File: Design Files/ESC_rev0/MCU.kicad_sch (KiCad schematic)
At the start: 39 parts, among them J1 Conn_01x08, J2 Conn_01x06, J3 Conn_01x03, SW1 SW_DIP_x01, U4 STM32F405RGTx, Y1 Crystal

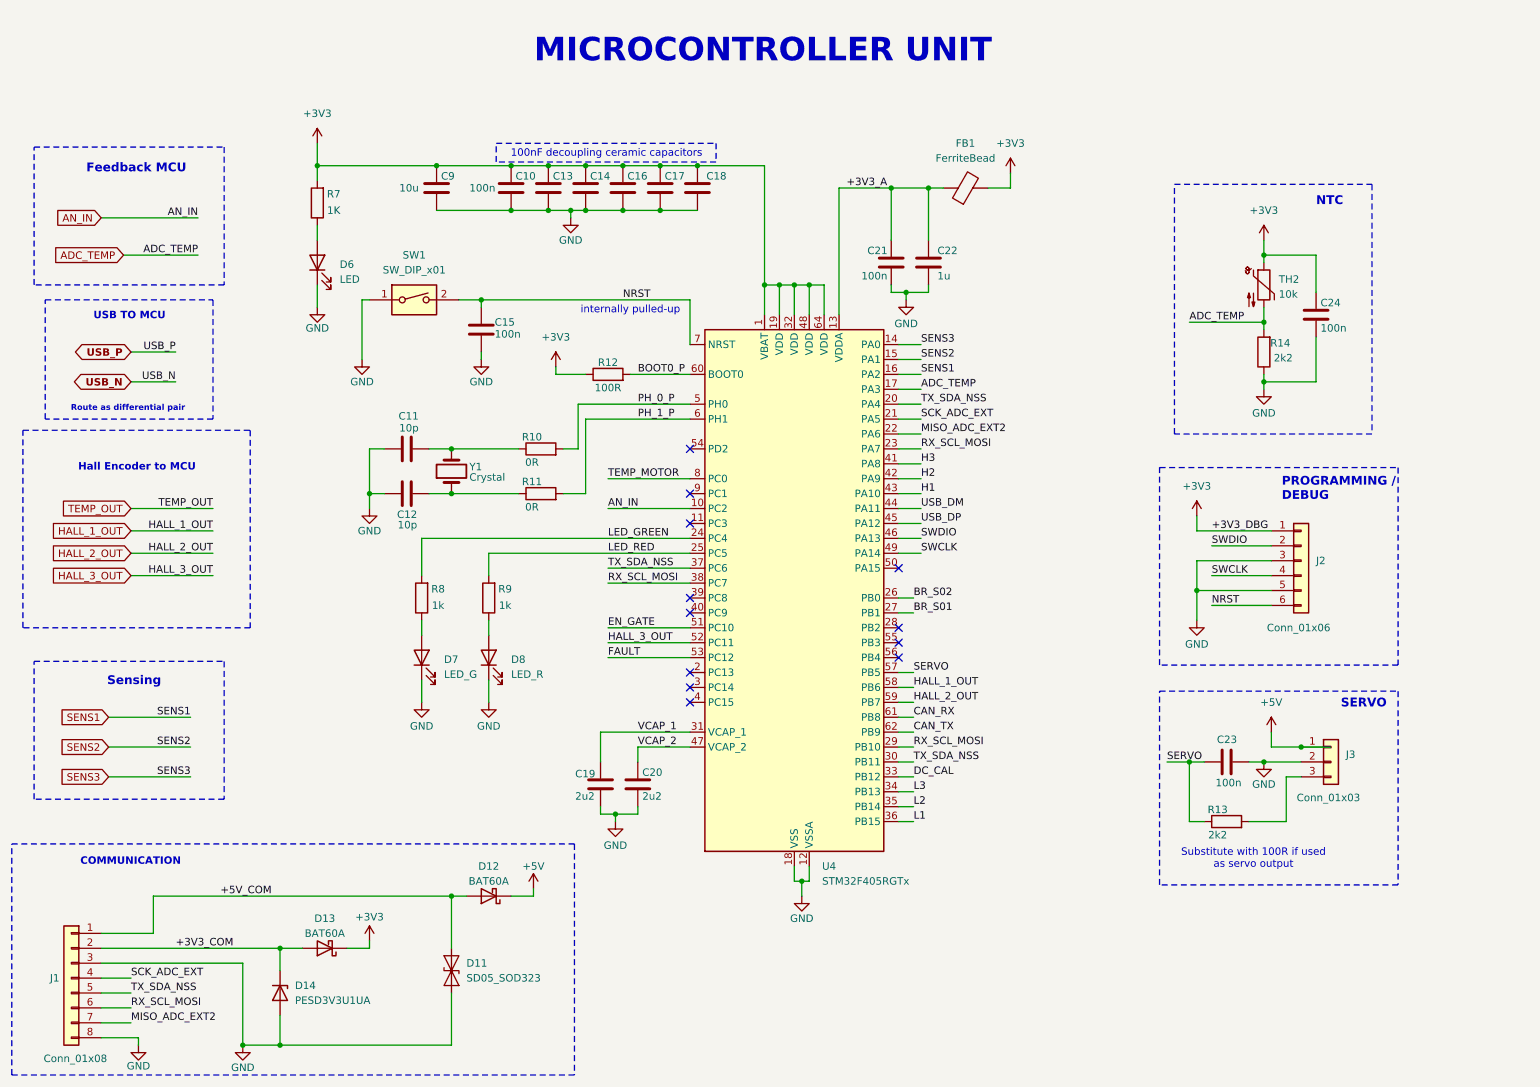
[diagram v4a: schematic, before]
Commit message: update 13
assigned all footprints (provisionally) and imported them - errors and warning occurred, must be corrected in the future
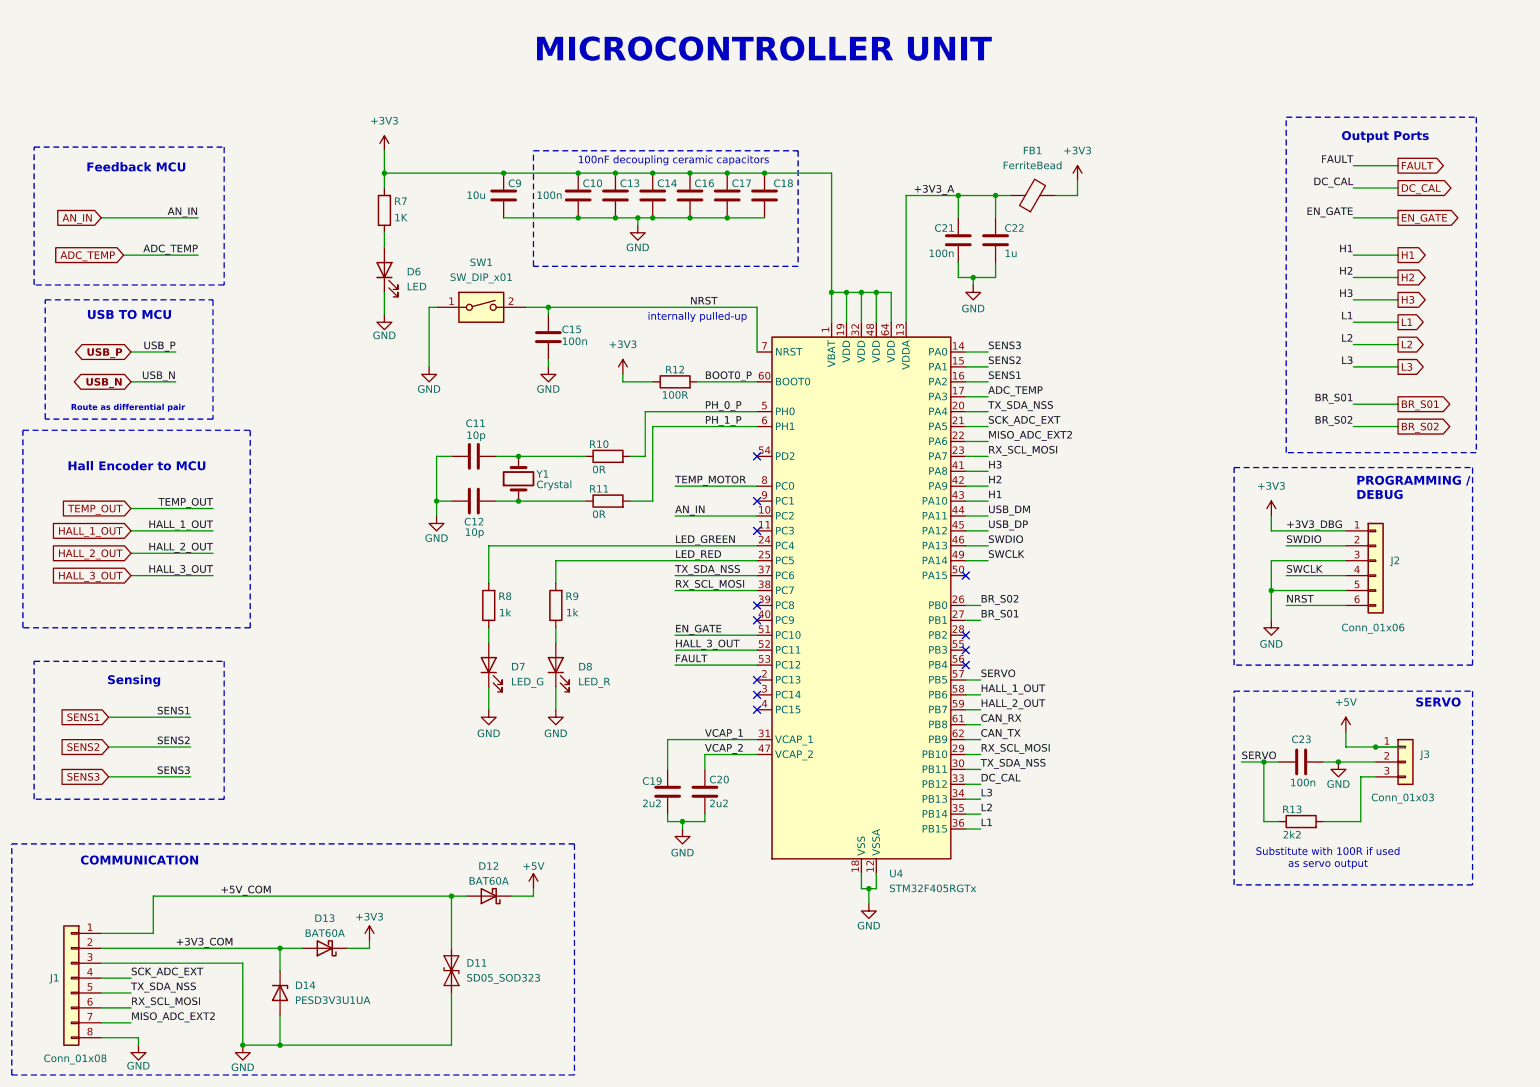
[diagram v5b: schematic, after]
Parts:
- removed C24: 100n, Capacitor_SMD:C_0201_0603Metric, symbol Device:C
- removed R14: 2k2, symbol Device:R
- removed TH2: 10k, symbol Device:Thermistor_NTC
- J1: footprint (none) -> Connector_PinHeader_2.00mm:PinHeader_1x08_P2.00mm_Vertical
- J2: footprint (none) -> Connector_PinHeader_2.00mm:PinHeader_1x06_P2.00mm_Vertical
- J3: footprint (none) -> Connector_PinHeader_2.00mm:PinHeader_1x03_P2.00mm_Vertical
- R10, R11, R12, R13, R7, R8, R9: footprint (none) -> Resistor_SMD:R_0603_1608Metric
- SW1: footprint (none) -> Button_Switch_SMD:SW_DIP_SPSTx01_Slide_6.7x4.1mm_W6.73mm_P2.54mm_LowProfile_JPin
- Y1: footprint (none) -> Crystal:Crystal_HC50_Vertical
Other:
- note added: "Output Ports"
- note removed: "NTC"
- moved on the sheet: C10, C11, C12, C13, C14, C15, C16, C17, C18, C19, C20, C21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

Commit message: update 14
Circuits separated by schematic pages. Replaced crystal footprint.
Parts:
- Y1: footprint Crystal:Crystal_HC50_Vertical -> Crystal:Crystal_SMD_0603-4Pin_6.0x3.5mm_HandSoldering
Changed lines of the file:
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@@
 			)
 		)
-		(property "Footprint" "Crystal:Crystal_HC50_Vertical"
+		(property "Footprint" "Crystal:Crystal_SMD_0603-4Pin_6.0x3.5mm_HandSoldering"
 			(at 104.14 93.98 0)
 			(effects

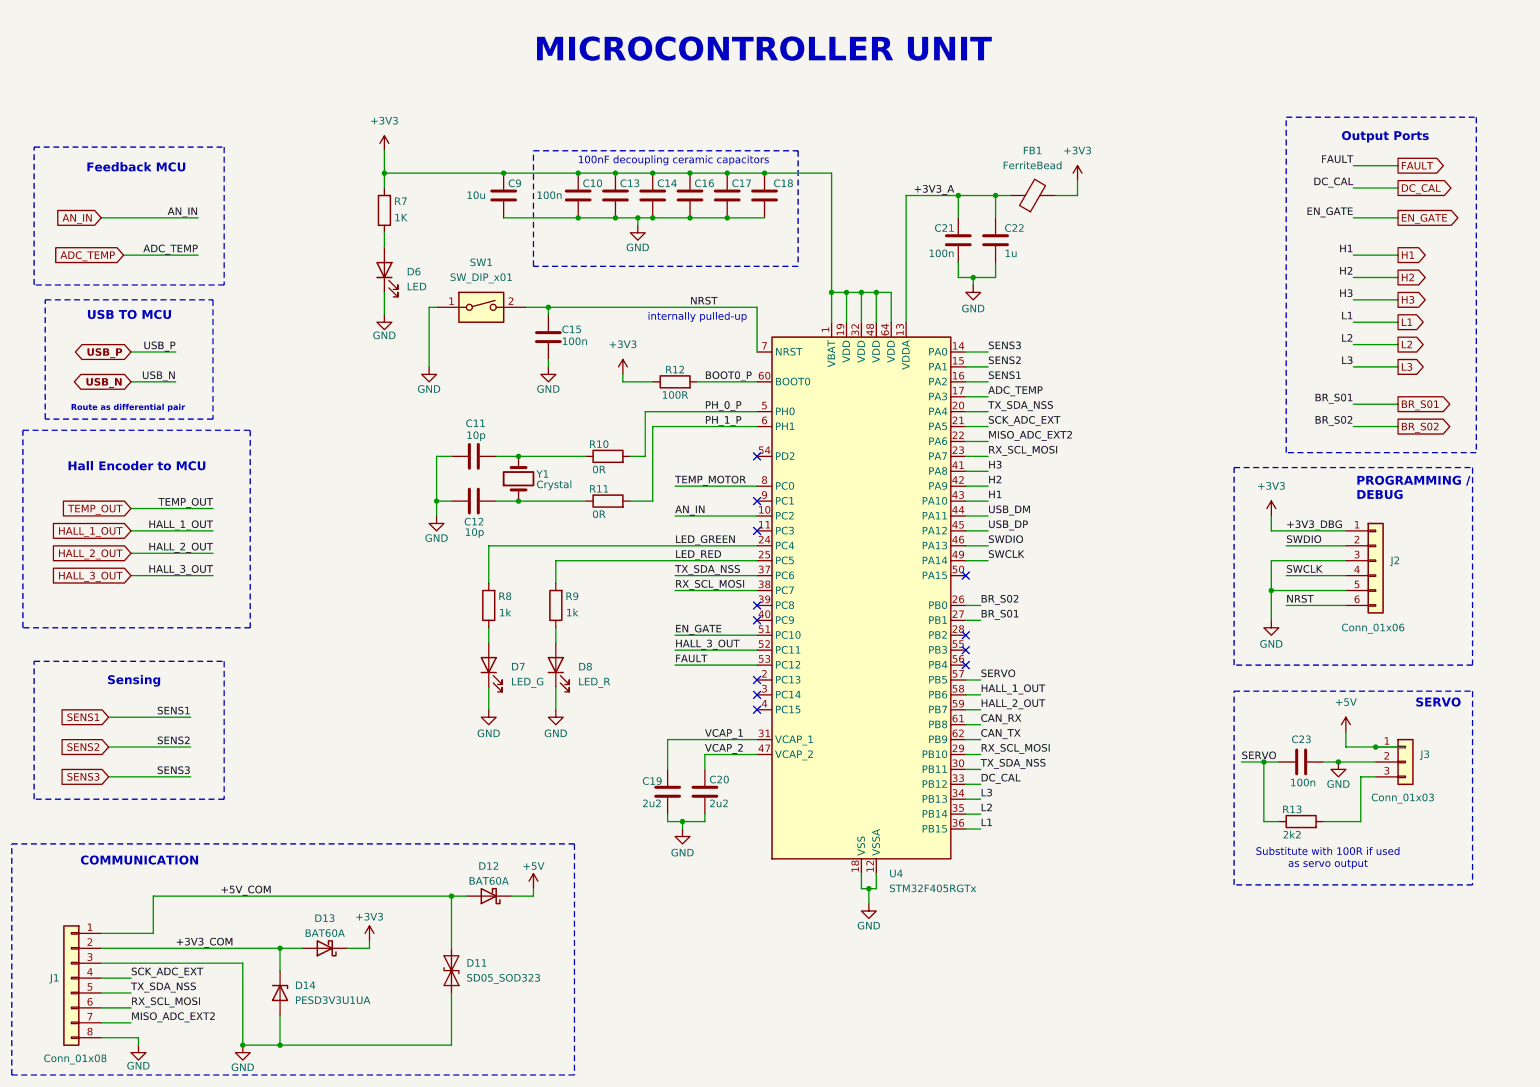
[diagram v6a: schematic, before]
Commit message: update 15
Simple connectors replaced by smd connectors (downloaded). Connectors were placed in edges of the board.
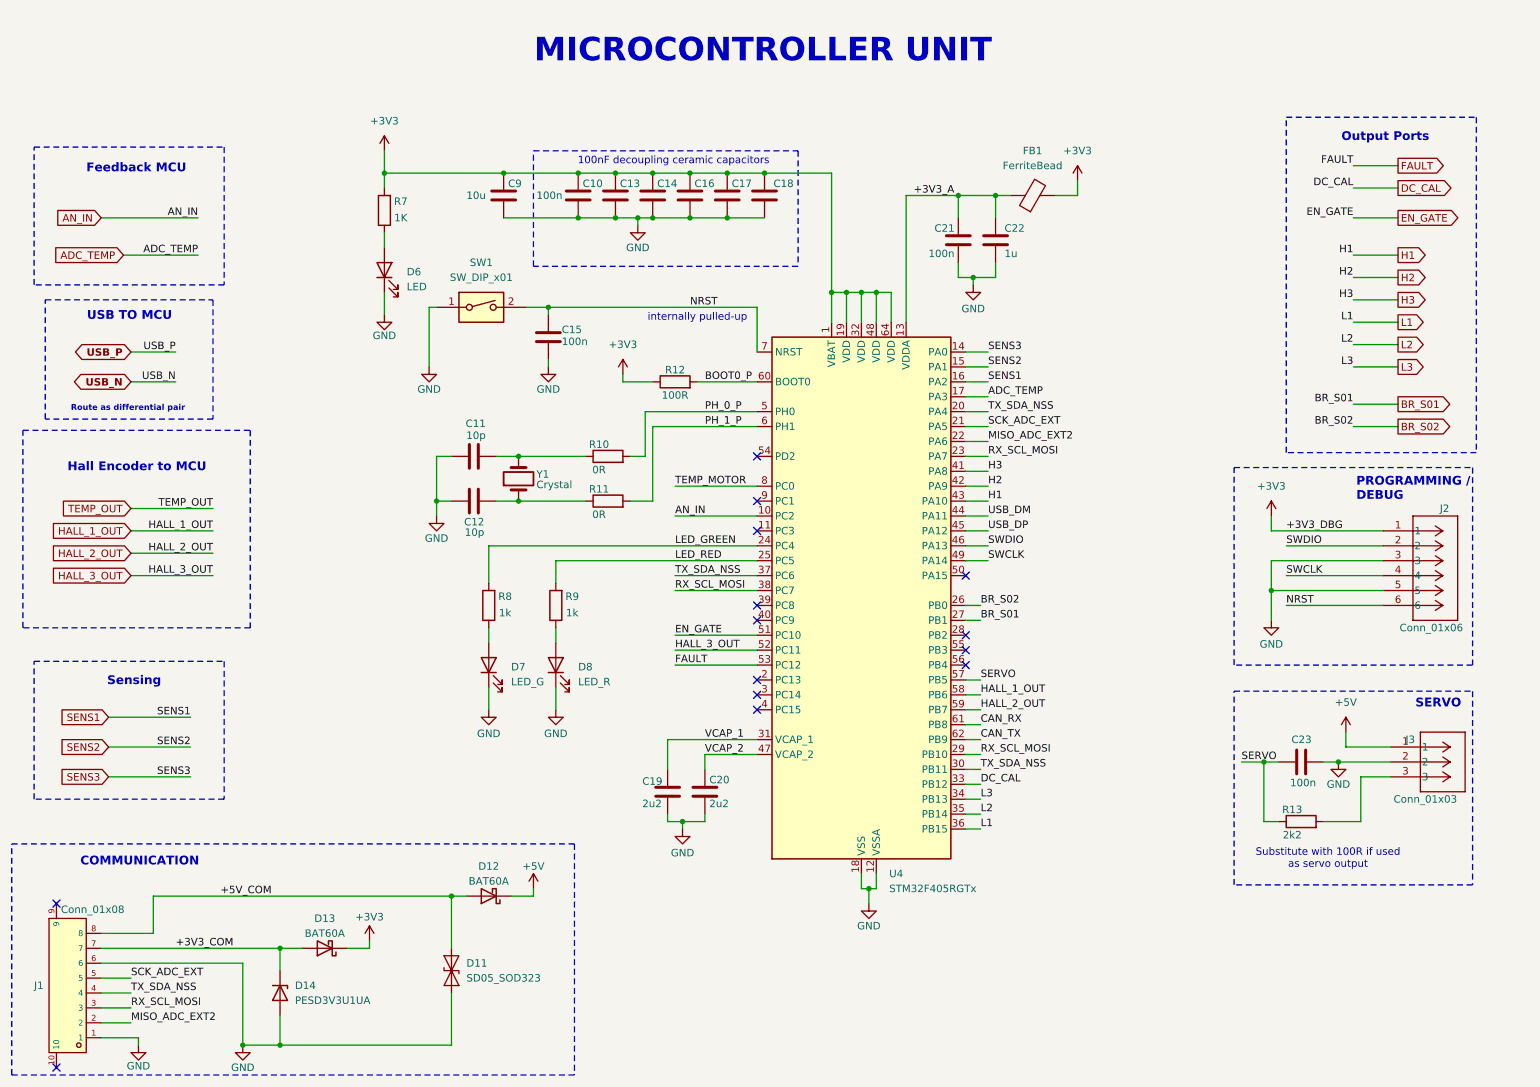
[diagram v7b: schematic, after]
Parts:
- J1: footprint Connector_PinHeader_2.00mm:PinHeader_1x08_P2.00mm_Vertical -> HX25003-8AWB:CONN-SMD_8P-P2.50_HX25003-8AWB; symbol Connector_Generic:Conn_01x08 -> HX25003-8AWB:HX25003-8AWB; LCSC (none) -> C442367
- J2: footprint Connector_PinHeader_2.00mm:PinHeader_1x06_P2.00mm_Vertical -> CONN_S6B-XH-SM4-TB_JST; symbol Connector_Generic:Conn_01x06 -> S6B-XH-SM4-TB:S6B-XH-SM4-TB
- J3: footprint Connector_PinHeader_2.00mm:PinHeader_1x03_P2.00mm_Vertical -> CONN3_S3B-XH_JST; symbol Connector_Generic:Conn_01x03 -> S3B-XH-SM4-TB:S3B-XH-SM4-TB
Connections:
- net +3V3_COM: now also J1.7; no longer J1.2 (Pin_2)
- net +5V_COM: now also J1.8; no longer J1.1 (Pin_1)
- net GND: now also J1.1, J1.6; no longer J1.3 (Pin_3), J1.8 (Pin_8)
- net MISO_ADC_EXT2: now also J1.2; no longer J1.7 (Pin_7)
- net RX_SCL_MOSI: now also J1.3; no longer J1.6 (Pin_6)
- net SCK_ADC_EXT: now also J1.5; no longer J1.4 (Pin_4)
- net TX_SDA_NSS: now also J1.4; no longer J1.5 (Pin_5)
- no-connect marks 12 -> 14
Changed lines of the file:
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@@
 	)
 	(junction
-		(at 250.19 139.7)
-		(diameter 0)
-		(color 0 0 0 0)
-	)
-	(junction
 		(at 114.3 41.91)
 		(diameter 0)
@@
 	)
 	(no_connect
+		(at 25.4 166.37)
+	)
+	(no_connect
 		(at 144.78 115.57)
 	)
@@
 	)
 	(no_connect
+		(at 25.4 194.31)
+	)
+	(no_connect
 		(at 144.78 133.35)
 	)
@@
 	(wire
 		(pts
+			(xy 245.11 139.7) (xy 252.73 139.7)
+		)
+		(stroke
+			(width 0)
+			(type default)
+		)
+	)
+	(wire
+		(pts
 			(xy 157.48 41.91) (xy 157.48 62.23)
 		)
@@
 	(wire
 		(pts
-			(xy 232.41 113.03) (xy 245.11 113.03)
+			(xy 232.41 113.03) (xy 251.46 113.03)
 		)
 		(stroke
@@
 	(wire
 		(pts
-			(xy 243.84 142.24) (xy 250.19 142.24)
+			(xy 243.84 142.24) (xy 252.73 142.24)
 		)
 		(stroke
@@
 	(wire
 		(pts
-			(xy 255.27 139.7) (xy 250.19 139.7)
-		)
-		(stroke
-			(width 0)
-			(type default)
-		)
-	)
-	(wire
-		(pts
 			(xy 165.1 62.23) (xy 165.1 67.31)
 		)
@@
 	(wire
 		(pts
-			(xy 234.95 115.57) (xy 245.11 115.57)
+			(xy 234.95 115.57) (xy 251.46 115.57)
 		)
 		(stroke
@@
 	(wire
 		(pts
-			(xy 234.95 110.49) (xy 245.11 110.49)
+			(xy 234.95 110.49) (xy 251.46 110.49)
 		)
 		(stroke
@@
 	(wire
 		(pts
-			(xy 247.65 144.78) (xy 250.19 144.78)
+			(xy 247.65 144.78) (xy 252.73 144.78)
 		)
 		(stroke
@@
 	(wire
 		(pts
-			(xy 250.19 139.7) (xy 245.11 139.7)
-		)
-		(stroke
-			(width 0)
-			(type default)
-		)
-	)
-	(wire
-		(pts
 			(xy 120.65 41.91) (xy 127 41.91)
 		)
@@
 	(wire
 		(pts
-			(xy 234.95 105.41) (xy 245.11 105.41)
+			(xy 234.95 105.41) (xy 251.46 105.41)
 		)
 		(stroke
@@
 	(wire
 		(pts
-			(xy 57.15 176.53) (xy 33.02 176.53)
+			(xy 180.34 133.35) (xy 182.88 133.35)
 		)
 		(stroke
@@
 	(wire
 		(pts
-			(xy 180.34 133.35) (xy 182.88 133.35)
+			(xy 241.3 142.24) (xy 243.84 142.24)
 		)
 		(stroke
@@
 	(wire
 		(pts
-			(xy 241.3 142.24) (xy 243.84 142.24)
+			(xy 227.33 142.24) (xy 231.14 142.24)
 		)
 		(stroke
@@
 	(wire
 		(pts
-			(xy 227.33 142.24) (xy 231.14 142.24)
+			(xy 33.02 186.69) (xy 38.1 186.69)
 		)
 		(stroke
@@
 	(wire
 		(pts
-			(xy 33.02 186.69) (xy 38.1 186.69)
+			(xy 63.5 190.5) (xy 57.15 190.5)
 		)
 		(stroke
@@
 	(wire
 		(pts
-			(xy 63.5 190.5) (xy 57.15 190.5)
+			(xy 33.02 176.53) (xy 57.15 176.53)
 		)
 		(stroke
@@
 	(wire
 		(pts
-			(xy 245.11 107.95) (xy 232.41 107.95)
+			(xy 232.41 107.95) (xy 251.46 107.95)
 		)
 		(stroke
@@
 	(wire
 		(pts
-			(xy 245.11 102.87) (xy 232.41 102.87)
+			(xy 232.41 102.87) (xy 251.46 102.87)
 		)
 		(stroke
@@
 	)
 	(symbol
-		(lib_id "Connector_Generic:Conn_01x06")
-		(at 250.19 107.95 0)
+		(lib_id "S6B-XH-SM4-TB:S6B-XH-SM4-TB")
+		(at 251.46 102.87 0)
 		(unit 1)
 		(exclude_from_sim no)
@@
 		(dnp no)
 		(property "Reference" "J2"
-			(at 252.73 107.9499 0)
+			(at 261.112 99.06 0)
 			(effects
 				(font
@@
 		)
 		(property "Value" "Conn_01x06"
-			(at 244.348 119.38 0)
+			(at 254.254 119.38 0)
 			(effects
 				(font
@@
 			)
 		)
-		(property "Footprint" "Connector_PinHeader_2.00mm:PinHeader_1x06_P2.00mm_Vertical"
-			(at 250.19 107.95 0)
+		(property "Footprint" "CONN_S6B-XH-SM4-TB_JST"
+			(at 254.762 119.634 0)
 			(effects
 				(font
 					(size 1.27 1.27)
+					(italic yes)
 				)
 				(hide yes)
 			)
 		)
-		(property "Datasheet" "~"
-			(at 250.19 107.95 0)
+		(property "Datasheet" "S6B-XH-SM4-TB"
+			(at 249.174 99.314 0)
 			(effects
 				(font
 					(size 1.27 1.27)
+					(italic yes)
 				)
 				(hide yes)
@@
 		)
 		(property "Description" "Generic connector, single row, 01x06, script generated (kicad-library-utils/schlib/autogen/connector/)"
-			(at 250.19 107.95 0)
+			(at 251.46 102.87 0)
 			(effects
 				(font
@@
 	)
 	(symbol
-		(lib_id "Connector_Generic:Conn_01x03")
-		(at 255.27 142.24 0)
+		(lib_id "S3B-XH-SM4-TB:S3B-XH-SM4-TB")
+		(at 252.73 139.7 0)
 		(unit 1)
 		(exclude_from_sim no)
@@
 		(dnp no)
 		(property "Reference" "J3"
-			(at 257.81 140.9699 0)
+			(at 255.27 138.4299 0)
 			(effects
 				(font
@@
 		)
 		(property "Value" "Conn_01x03"
-			(at 249.428 148.336 0)
+			(at 253.238 148.59 0)
 			(effects
 				(font
@@
 			)
 		)
-		(property "Footprint" "Connector_PinHeader_2.00mm:PinHeader_1x03_P2.00mm_Vertical"
-			(at 255.27 142.24 0)
+		(property "Footprint" "CONN3_S3B-XH_JST"
+			(at 252.73 139.7 0)
 			(effects
 				(font
 					(size 1.27 1.27)
+					(italic yes)
 				)
 				(hide yes)
 			)
 		)
-		(property "Datasheet" "~"
-			(at 255.27 142.24 0)
+		(property "Datasheet" "S3B-XH-SM4-TB"
+			(at 252.73 139.7 0)
 			(effects
 				(font
 					(size 1.27 1.27)
+					(italic yes)
 				)
 				(hide yes)
@@
 		)
 		(property "Description" "Generic connector, single row, 01x03, script generated (kicad-library-utils/schlib/autogen/connector/)"
-			(at 255.27 142.24 0)
+			(at 252.73 139.7 0)
 			(effects
 				(font
@@
 	)
 	(symbol
-		(lib_id "Connector_Generic:Conn_01x08")
-		(at 27.94 179.07 0)
-		(mirror y)
+		(lib_id "HX25003-8AWB:HX25003-8AWB")
+		(at 27.94 180.34 0)
+		(mirror x)
 		(unit 1)
 		(exclude_from_sim no)
@@
 		(dnp no)
 		(property "Reference" "J1"
-			(at 25.908 179.07 0)
+			(at 21.59 180.34 0)
 			(effects
 				(font
@@
 		)
 		(property "Value" "Conn_01x08"
-			(at 34.036 192.786 0)
+			(at 26.162 167.386 0)
 			(effects
 				(font
@@
 			)
 		)
-		(property "Footprint" "Connector_PinHeader_2.00mm:PinHeader_1x08_P2.00mm_Vertical"
-			(at 27.94 179.07 0)
+		(property "Footprint" "HX25003-8AWB:CONN-SMD_8P-P2.50_HX25003-8AWB"
+			(at 26.162 156.21 0)
 			(effects
 				(font
 					(size 1.27 1.27)
+					(italic yes)
 				)
 				(hide yes)
 			)
 		)
-		(property "Datasheet" "~"
-			(at 27.94 179.07 0)
+		(property "Datasheet" "https://list.szlcsc.com/catalog/11068.html"
+			(at 6.35 158.496 0)
 			(effects
 				(font
 					(size 1.27 1.27)
 				)
+				(justify left)
 				(hide yes)
 			)
 		)
 		(property "Description" "Generic connector, single row, 01x08, script generated (kicad-library-utils/schlib/autogen/connector/)"
-			(at 27.94 179.07 0)
+			(at 29.21 180.34 0)
+			(effects
+				(font
+					(size 1.27 1.27)
+				)
+				(hide yes)
+			)
+		)
+		(property "LCSC" "C442367"
+			(at 19.812 180.34 0)
 			(effects
 				(font
@@
 		(pin "6"
 		)
+		(pin "9"
+		)
+		(pin "10"
+		)
 		(instances
